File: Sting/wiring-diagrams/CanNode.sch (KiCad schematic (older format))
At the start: 52 parts

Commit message: fixed some stuff
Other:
- note added: "CAN_OUT is a pass through connector for CAN."
- note added: "Full schematics with reference numbers are in the \ncan_sensor folder in the supermileagehw git repo at \nhttps://github.com/HEEV/supermileageHW"
- note added: "On Chip Debugging connector.\nUse a stm32 Discovery board, or a STLinkv2 board."
- note added: "R2, R5 and R3,R6 form a resistor divider for \nattenuating input signals.\nR5 and R6 could be replaced by a capacitor for input \ndebouncing/low pass filter.\n\nD1, D2, D3, and D4 hopefully provide some sort of \nvoltage spike protection. However, I would not trust it\noverly much, as it depends on the current sinking ability of \nthe 3.3v regulator."
- note added: "To program through USB, hold down \nthe BOOT button and reset the uC."
- note removed: "Full schematics with reference numbers are in the \ncan_sensor folder in the supermileagehw git repo at \nhttps://bitbucket.org/nebk/supermileagehw"
- moved on the sheet: R

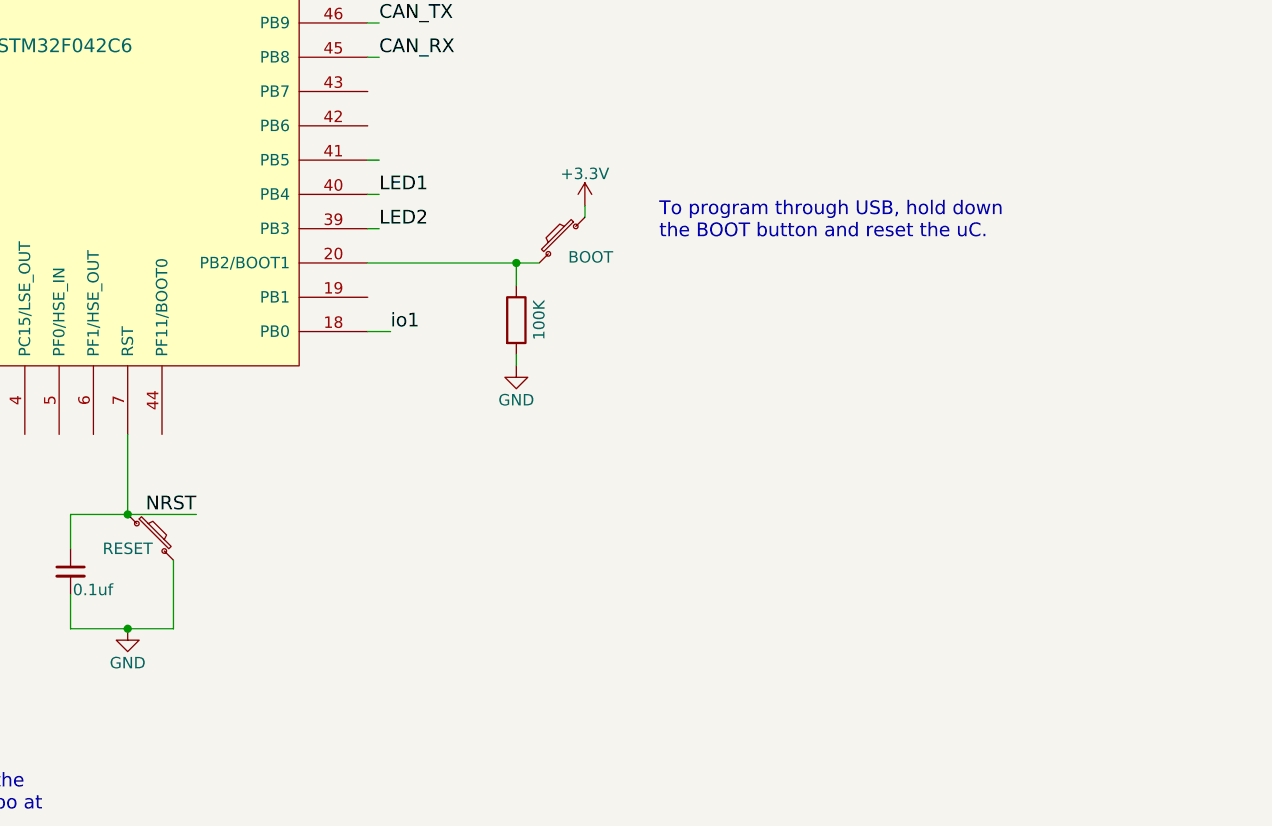
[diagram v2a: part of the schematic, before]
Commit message: fixed missing parts updated sensor boards
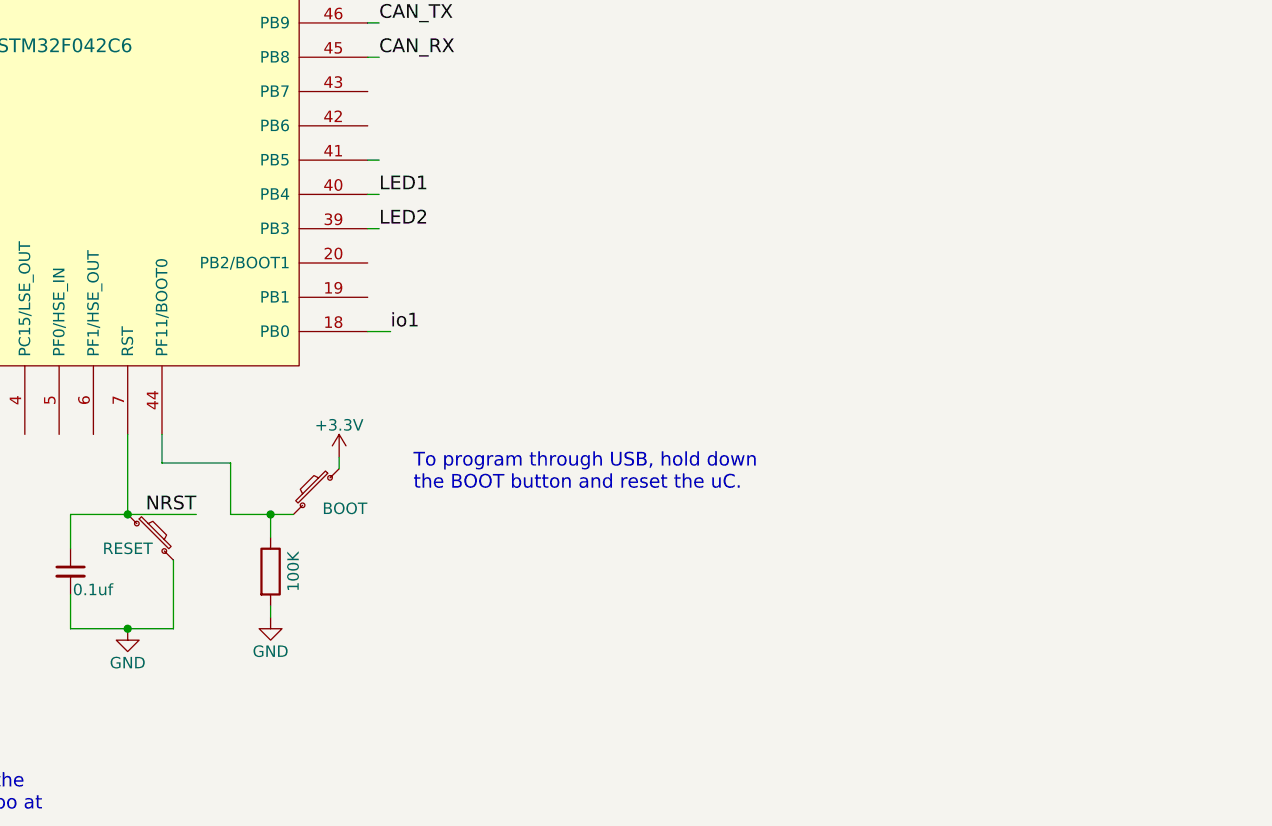
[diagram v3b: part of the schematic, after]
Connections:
- net at R?.1, SW?.2: now also U?.44 (PF11/BOOT0); no longer U?.20 (PB2/BOOT1)
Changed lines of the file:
@@
 $Descr USLetter 11000 8500
 encoding utf-8
-Sheet 10 14
+Sheet 8 14
 Title "Can Node"
 Date "2016-05-09"
@@
 AR Path="/5880E829/5880F9D7" Ref="P?"  Part="1"
 AR Path="/58828DB7/5880F9D7" Ref="P?"  Part="1"
+AR Path="/5880F9D7" Ref="P?"  Part="1"
 F 0 "P?" V 975 7225 50  0001 C CNN
 F 1 "USB" H 1275 7425 50  0000 C CNN
@@
 L SW_PUSH_SMALL SW?
 U 1 1 5880F9DB
-P 7350 5300
+P 6275 6400
 AR Path="/5880E829/5880F9DB" Ref="SW?"  Part="1"
 AR Path="/58828DB7/5880F9DB" Ref="SW?"  Part="1"
-F 0 "SW?" H 7500 5410 50  0001 C CNN
-F 1 "BOOT" H 7225 5225 50  0000 C CNN
-F 2 "Buttons_Switches_SMD:SW_SPST_FSMSM" V 7350 5300 50  0001 C CNN
-F 3 "" H 7350 5300 50  0000 C CNN
-	1    7350 5300
+F 0 "SW?" H 6425 6510 50  0001 C CNN
+F 1 "BOOT" H 6150 6325 50  0000 C CNN
+F 2 "Buttons_Switches_SMD:SW_SPST_FSMSM" V 6275 6400 50  0001 C CNN
+F 3 "" H 6275 6400 50  0000 C CNN
+	1    6275 6400
 	-1   0    0    -1
 $EndComp
@@
 L GND #PWR?
 U 1 1 5880F9DC
-P 7150 5850
+P 6075 6950
 AR Path="/5880E829/5880F9DC" Ref="#PWR?"  Part="1"
 AR Path="/58828DB7/5880F9DC" Ref="#PWR?"  Part="1"
-F 0 "#PWR?" H 7150 5600 50  0001 C CNN
-F 1 "GND" H 7150 5700 50  0000 C CNN
-F 2 "" H 7150 5850 50  0000 C CNN
-F 3 "" H 7150 5850 50  0000 C CNN
-	1    7150 5850
+F 0 "#PWR?" H 6075 6700 50  0001 C CNN
+F 1 "GND" H 6075 6800 50  0000 C CNN
+F 2 "" H 6075 6950 50  0000 C CNN
+F 3 "" H 6075 6950 50  0000 C CNN
+	1    6075 6950
 	1    0    0    -1
 $EndComp
@@
 L +3.3V #PWR?
 U 1 1 5880F9DD
-P 7450 5150
+P 6375 6250
 AR Path="/5880E829/5880F9DD" Ref="#PWR?"  Part="1"
 AR Path="/58828DB7/5880F9DD" Ref="#PWR?"  Part="1"
-F 0 "#PWR?" H 7450 5000 50  0001 C CNN
-F 1 "+3.3V" H 7450 5290 50  0000 C CNN
-F 2 "" H 7450 5150 50  0000 C CNN
-F 3 "" H 7450 5150 50  0000 C CNN
-	1    7450 5150
+F 0 "#PWR?" H 6375 6100 50  0001 C CNN
+F 1 "+3.3V" H 6375 6390 50  0000 C CNN
+F 2 "" H 6375 6250 50  0000 C CNN
+F 3 "" H 6375 6250 50  0000 C CNN
+	1    6375 6250
 	1    0    0    -1
 $EndComp
@@
 L R R?
 U 1 1 5880F9E2
-P 7150 5650
+P 6075 6750
 AR Path="/5880E829/5880F9E2" Ref="R?"  Part="1"
 AR Path="/58828DB7/5880F9E2" Ref="R?"  Part="1"
-F 0 "R?" V 7250 5650 50  0001 C CNN
-F 1 "100K" V 7250 5650 50  0000 C CNN
-F 2 "Resistors_SMD:R_0603_HandSoldering" H 7080 5650 50  0001 C CNN
-F 3 "" H 7150 5650 50  0000 C CNN
-F 4 "Mouser" V 7150 5650 60  0001 C CNN "Distributor"
-F 5 "71-CRCW0603-100K-E3" V 7150 5650 60  0001 C CNN "PN"
-	1    7150 5650
+F 0 "R?" V 6175 6750 50  0001 C CNN
+F 1 "100K" V 6175 6750 50  0000 C CNN
+F 2 "Resistors_SMD:R_0603_HandSoldering" H 6005 6750 50  0001 C CNN
+F 3 "" H 6075 6750 50  0000 C CNN
+F 4 "Mouser" V 6075 6750 60  0001 C CNN "Distributor"
+F 5 "71-CRCW0603-100K-E3" V 6075 6750 60  0001 C CNN "PN"
+	1    6075 6750
 	1    0    0    -1
 $EndComp
@@
 	5200 6850 5200 7000
 Wire Wire Line
-	6500 5400 7250 5400
-Wire Wire Line
-	7150 5500 7150 5400
-Connection ~ 7150 5400
-Wire Wire Line
-	7150 5850 7150 5800
-Wire Wire Line
-	7450 5150 7450 5200
+	6075 6600 6075 6500
+Connection ~ 6075 6500
+Wire Wire Line
+	6075 6950 6075 6900
+Wire Wire Line
+	6375 6250 6375 6300
 Connection ~ 5450 6500
 Wire Wire Line
@@
 Text Notes 800  6025 0    60   ~ 0
 On Chip Debugging connector.\nUse a stm32 Discovery board, or a STLinkv2 board.
-Text Notes 7775 5300 0    60   ~ 0
+Text Notes 6700 6400 0    60   ~ 0
 To program through USB, hold down \nthe BOOT button and reset the uC.
+Wire Wire Line
+	6175 6500 5900 6500
+Wire Wire Line
+	5900 6500 5900 6275
+Wire Wire Line
+	5900 6275 5600 6275
+Wire Wire Line
+	5600 6275 5600 6150
 $EndSCHEMATC

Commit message: Moved where the relay to turn on the starter relay gets power from
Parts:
- P?: symbol USB_OTG -> USB_OTG-RESCUE-Wiring_Diagram_v2
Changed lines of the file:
@@
 EESchema Schematic File Version 2
+LIBS:Wiring Diagram v2-rescue
 LIBS:power
 LIBS:device
@@
 $EndComp
 $Comp
-L USB_OTG P?
+L USB_OTG-RESCUE-Wiring_Diagram_v2 P?
 U 1 1 5880F9D7
 P 1275 7225
